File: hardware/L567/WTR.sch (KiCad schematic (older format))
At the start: 14 parts, among them Q4 2N3014

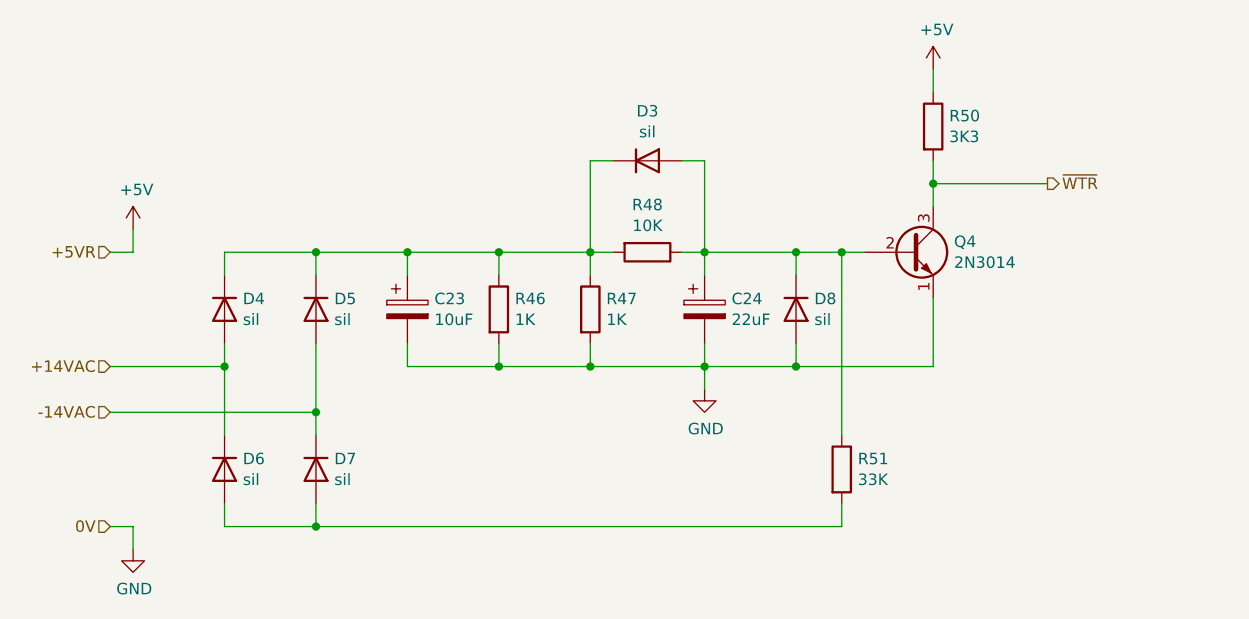
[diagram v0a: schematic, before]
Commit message: some power supply updates
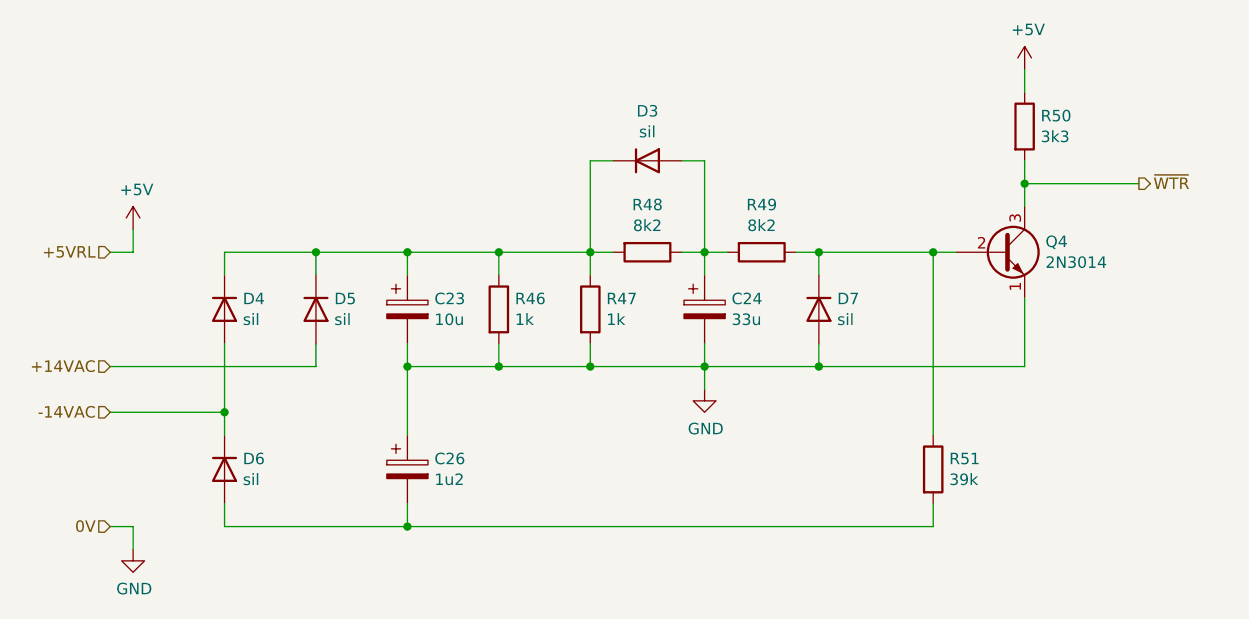
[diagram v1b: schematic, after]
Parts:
- removed D7: sil, symbol Device:D
- added C26: 1u2, symbol Device:CP
- added R49: 8k2, symbol Device:R
- C23: value 10uF -> 10u
- C24: value 22uF -> 33u; Partnumber 330-4015 -> 330-4019
- R46, R47: value 1K -> 1k
- R48: value 10K -> 8k2; Partnumber 330-4010 -> (none); Tolerance (none) -> 5%
- R50: value 3K3 -> 3k3
- R51: value 33K -> 39k; Tolerance (none) -> 5%
- renumbered D8 to D7
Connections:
- net +14VAC: now also D5.2 (A); no longer D4.2 (A), D6.1 (K)
- net -14VAC: now also D4.2 (A), D6.1 (K); no longer D5.2 (A)
- net GND: now also C26.1
- net at D6.2 (A), R51.2: now also C26.2
- net at C24.1, D3.2 (A), R48.1: now also R49.2; no longer D7.1 (K), Q4.2 (B), R51.1
- new net: D7.1 (K), Q4.2 (B), R49.1, R51.1
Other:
- moved on the sheet: D7, Q4, R50, R51
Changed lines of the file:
@@
 $Descr A4 11693 8268
 encoding utf-8
-Sheet 2 2
+Sheet 2 4
 Title ""
 Date ""
@@
 	6000 2600 6100 2600
 Wire Wire Line
-	6100 3000 6500 3000
+	6500 3000 6600 3000
 Connection ~ 6100 3000
 Wire Wire Line
 	6100 3000 6100 3100
 Wire Wire Line
-	6500 3000 6700 3000
-Connection ~ 6500 3000
-Wire Wire Line
-	6500 3000 6500 3100
+	6600 3000 7100 3000
+Connection ~ 6600 3000
+Wire Wire Line
+	6600 3000 6600 3100
 Wire Wire Line
 	6000 3000 6100 3000
@@
 Wire Wire Line
 	5700 3000 5600 3000
-Connection ~ 6500 3500
-Wire Wire Line
-	7100 3500 7100 3200
-Wire Wire Line
-	6500 3500 7100 3500
+Connection ~ 6600 3500
+Wire Wire Line
+	7500 3500 7500 3200
+Wire Wire Line
+	6600 3500 7500 3500
 Connection ~ 6100 3500
 Wire Wire Line
-	6500 3500 6500 3400
-Wire Wire Line
-	6100 3500 6500 3500
+	6600 3500 6600 3400
+Wire Wire Line
+	6100 3500 6600 3500
 Connection ~ 5600 3500
 Wire Wire Line
@@
 	4800 3000 4800 3100
 Text HLabel 3500 3000 0    50   Input ~ 0
-+5VR
++5VRL
 Text HLabel 3500 4200 0    50   Input ~ 0
 0V
-Text HLabel 7600 2700 2    50   Output ~ 0
+Text HLabel 8000 2700 2    50   Output ~ 0
 ~WTR
 $Comp
 L Device:R R50
 U 1 1 6056D046
-P 7100 2450
-F 0 "R50" H 7170 2496 50  0000 L CNN
-F 1 "3K3" H 7170 2405 50  0000 L CNN
-F 2 "" V 7030 2450 50  0001 C CNN
-F 3 "~" H 7100 2450 50  0001 C CNN
-F 4 "330-3033" H 7100 2450 50  0001 C CNN "Partnumber"
-F 5 "1/4W" H 7100 2450 50  0001 C CNN "Power"
-	1    7100 2450
+P 7500 2450
+F 0 "R50" H 7570 2496 50  0000 L CNN
+F 1 "3k3" H 7570 2405 50  0000 L CNN
+F 2 "" V 7430 2450 50  0001 C CNN
+F 3 "~" H 7500 2450 50  0001 C CNN
+F 4 "330-3033" H 7500 2450 50  0001 C CNN "Partnumber"
+F 5 "1/4W" H 7500 2450 50  0001 C CNN "Power"
+	1    7500 2450
 	1    0    0    -1
 $EndComp
@@
 L Device:Q_NPN_EBC Q4
 U 1 1 6056C773
-P 7000 3000
-F 0 "Q4" H 7191 3046 50  0000 L CNN
-F 1 "2N3014" H 7191 2955 50  0000 L CNN
-F 2 "" H 7200 3100 50  0001 C CNN
-F 3 "~" H 7000 3000 50  0001 C CNN
-F 4 "375-0017" H 7000 3000 50  0001 C CNN "Partnumber"
-	1    7000 3000
+P 7400 3000
+F 0 "Q4" H 7591 3046 50  0000 L CNN
+F 1 "2N3014" H 7591 2955 50  0000 L CNN
+F 2 "" H 7600 3100 50  0001 C CNN
+F 3 "~" H 7400 3000 50  0001 C CNN
+F 4 "375-0017" H 7400 3000 50  0001 C CNN "Partnumber"
+	1    7400 3000
 	1    0    0    -1
 $EndComp
@@
 L Device:R R51
 U 1 1 6056AAF1
-P 6700 3950
-F 0 "R51" H 6770 3996 50  0000 L CNN
-F 1 "33K" H 6770 3905 50  0000 L CNN
-F 2 "" V 6630 3950 50  0001 C CNN
-F 3 "~" H 6700 3950 50  0001 C CNN
-F 4 "330-4033" H 6700 3950 50  0001 C CNN "Partnumber"
-F 5 "1/4W" H 6700 3950 50  0001 C CNN "Power"
-	1    6700 3950
+P 7100 3950
+F 0 "R51" H 7170 3996 50  0000 L CNN
+F 1 "39k" H 7170 3905 50  0000 L CNN
+F 2 "" V 7030 3950 50  0001 C CNN
+F 3 "~" H 7100 3950 50  0001 C CNN
+F 4 "330-4033" H 7100 3950 50  0001 C CNN "Partnumber"
+F 5 "1/4W" H 7100 3950 50  0001 C CNN "Power"
+F 6 "5%" H 7100 3950 50  0001 C CNN "Tolerance"
+	1    7100 3950
 	1    0    0    -1
 $EndComp
@@
 P 4800 3250
 F 0 "C23" H 4918 3296 50  0000 L CNN
-F 1 "10uF" H 4918 3205 50  0000 L CNN
+F 1 "10u" H 4918 3205 50  0000 L CNN
 F 2 "" H 4838 3100 50  0001 C CNN
 F 3 "~" H 4800 3250 50  0001 C CNN
@@
 $EndComp
 $Comp
-L Device:D D8
+L Device:D D7
 U 1 1 6056397D
-P 6500 3250
-F 0 "D8" V 6454 3330 50  0000 L CNN
-F 1 "sil" V 6545 3330 50  0000 L CNN
-F 2 "" H 6500 3250 50  0001 C CNN
-F 3 "~" H 6500 3250 50  0001 C CNN
-F 4 "380-1001" H 6500 3250 50  0001 C CNN "Partnumber"
-F 5 "Silicium" H 6500 3250 50  0001 C CNN "Technology"
-	1    6500 3250
+P 6600 3250
+F 0 "D7" V 6554 3330 50  0000 L CNN
+F 1 "sil" V 6645 3330 50  0000 L CNN
+F 2 "" H 6600 3250 50  0001 C CNN
+F 3 "~" H 6600 3250 50  0001 C CNN
+F 4 "380-1001" H 6600 3250 50  0001 C CNN "Partnumber"
+F 5 "Silicium" H 6600 3250 50  0001 C CNN "Technology"
+	1    6600 3250
 	0    1    1    0
 $EndComp
@@
 P 5850 3000
 F 0 "R48" V 5643 3000 50  0000 C CNN
-F 1 "10K" V 5734 3000 50  0000 C CNN
+F 1 "8k2" V 5734 3000 50  0000 C CNN
 F 2 "" V 5780 3000 50  0001 C CNN
 F 3 "~" H 5850 3000 50  0001 C CNN
-F 4 "330-4010" H 5850 3000 50  0001 C CNN "Partnumber"
+F 4 "" H 5850 3000 50  0001 C CNN "Partnumber"
 F 5 "1/4W" H 5850 3000 50  0001 C CNN "Power"
+F 6 "5%" H 5850 3000 50  0001 C CNN "Tolerance"
 	1    5850 3000
 	0    1    1    0
@@
 P 5600 3250
 F 0 "R47" H 5670 3296 50  0000 L CNN
-F 1 "1K" H 5670 3205 50  0000 L CNN
+F 1 "1k" H 5670 3205 50  0000 L CNN
 F 2 "" V 5530 3250 50  0001 C CNN
 F 3 "~" H 5600 3250 50  0001 C CNN
@@
 P 5200 3250
 F 0 "R46" H 5270 3296 50  0000 L CNN
-F 1 "1K" H 5270 3205 50  0000 L CNN
+F 1 "1k" H 5270 3205 50  0000 L CNN
 F 2 "" V 5130 3250 50  0001 C CNN
 F 3 "~" H 5200 3250 50  0001 C CNN
@@
 P 6100 3250
 F 0 "C24" H 6218 3296 50  0000 L CNN
-F 1 "22uF" H 6218 3205 50  0000 L CNN
+F 1 "33u" H 6218 3205 50  0000 L CNN
 F 2 "" H 6138 3100 50  0001 C CNN
 F 3 "~" H 6100 3250 50  0001 C CNN
-F 4 "330-4015" H 6100 3250 50  0001 C CNN "Partnumber"
+F 4 "330-4019" H 6100 3250 50  0001 C CNN "Partnumber"
 F 5 "Tantalum" H 6100 3250 50  0001 C CNN "Technology"
 F 6 "15V" H 6100 3250 50  0001 C CNN "Voltage"
@@
 $EndComp
 Wire Wire Line
-	4400 3700 4400 3800
-Connection ~ 4400 3700
-Wire Wire Line
-	3500 3700 4400 3700
-Wire Wire Line
-	4000 3500 4000 3800
-Connection ~ 4000 3500
-Wire Wire Line
-	3500 3500 4000 3500
-Wire Wire Line
-	4400 3400 4400 3700
-Wire Wire Line
-	4400 4200 4400 4100
-Wire Wire Line
-	4000 4200 4400 4200
+	3500 3500 4400 3500
+Wire Wire Line
+	4000 3700 4000 3800
+Connection ~ 4000 3700
+Wire Wire Line
+	3500 3700 4000 3700
+Wire Wire Line
+	4400 3400 4400 3500
 Wire Wire Line
 	4000 4100 4000 4200
 Wire Wire Line
-	4000 3400 4000 3500
+	4000 3400 4000 3700
 Wire Wire Line
 	4400 3000 4400 3100
@@
 Wire Wire Line
 	4000 3100 4000 3000
-$Comp
-L Device:D D7
-U 1 1 6055D71C
-P 4400 3950
-F 0 "D7" V 4354 4030 50  0000 L CNN
-F 1 "sil" V 4445 4030 50  0000 L CNN
-F 2 "" H 4400 3950 50  0001 C CNN
-F 3 "~" H 4400 3950 50  0001 C CNN
-F 4 "380-1004" H 4400 3950 50  0001 C CNN "Partnumber"
-F 5 "Silicium" H 4400 3950 50  0001 C CNN "Technology"
-	1    4400 3950
-	0    1    1    0
-$EndComp
 $Comp
 L Device:D D6
@@
 +14VAC
 Wire Wire Line
-	6700 3000 6700 3800
-Connection ~ 6700 3000
-Wire Wire Line
-	6700 3000 6800 3000
+	7100 3000 7100 3800
+Connection ~ 7100 3000
+Wire Wire Line
+	7100 3000 7200 3000
 Wire Wire Line
 	6100 3500 6100 3600
 Wire Wire Line
-	6700 4100 6700 4200
-Wire Wire Line
-	6700 4200 4400 4200
-Connection ~ 4400 4200
+	7100 4100 7100 4200
 $Comp
 L power:+5V #PWR0102
@@
 L power:+5V #PWR0104
 U 1 1 605DC71E
-P 7100 2200
-F 0 "#PWR0104" H 7100 2050 50  0001 C CNN
-F 1 "+5V" H 7115 2373 50  0000 C CNN
-F 2 "" H 7100 2200 50  0001 C CNN
-F 3 "" H 7100 2200 50  0001 C CNN
-	1    7100 2200
-	1    0    0    -1
-$EndComp
-Wire Wire Line
-	7100 2200 7100 2300
-Wire Wire Line
-	7100 2600 7100 2700
-Wire Wire Line
-	7100 2700 7600 2700
-Connection ~ 7100 2700
-Wire Wire Line
-	7100 2700 7100 2800
+P 7500 2200
+F 0 "#PWR0104" H 7500 2050 50  0001 C CNN
+F 1 "+5V" H 7515 2373 50  0000 C CNN
+F 2 "" H 7500 2200 50  0001 C CNN
+F 3 "" H 7500 2200 50  0001 C CNN
+	1    7500 2200
+	1    0    0    -1
+$EndComp
+Wire Wire Line
+	7500 2200 7500 2300
+Wire Wire Line
+	7500 2600 7500 2700
+Wire Wire Line
+	7500 2700 8000 2700
+Connection ~ 7500 2700
+Wire Wire Line
+	7500 2700 7500 2800
+Wire Wire Line
+	7100 4200 4800 4200
+$Comp
+L Device:CP C26
+U 1 1 607B5AED
+P 4800 3950
+F 0 "C26" H 4918 3996 50  0000 L CNN
+F 1 "1u2" H 4918 3905 50  0000 L CNN
+F 2 "" H 4838 3800 50  0001 C CNN
+F 3 "~" H 4800 3950 50  0001 C CNN
+F 4 "" H 4800 3950 50  0001 C CNN "Partnumber"
+F 5 "Tantalum" H 4800 3950 50  0001 C CNN "Technology"
+F 6 "35V" H 4800 3950 50  0001 C CNN "Voltage"
+	1    4800 3950
+	1    0    0    -1
+$EndComp
+Wire Wire Line
+	4800 3500 4800 3800
+Connection ~ 4800 3500
+Wire Wire Line
+	4800 4100 4800 4200
+Wire Wire Line
+	4000 4200 4800 4200
+$Comp
+L Device:R R49
+U 1 1 607C003B
+P 6350 3000
+F 0 "R49" V 6143 3000 50  0000 C CNN
+F 1 "8k2" V 6234 3000 50  0000 C CNN
+F 2 "" V 6280 3000 50  0001 C CNN
+F 3 "~" H 6350 3000 50  0001 C CNN
+F 4 "" H 6350 3000 50  0001 C CNN "Partnumber"
+F 5 "1/4W" H 6350 3000 50  0001 C CNN "Power"
+F 6 "5%" H 6350 3000 50  0001 C CNN "Tolerance"
+	1    6350 3000
+	0    1    1    0
+$EndComp
+Connection ~ 4800 4200
+Wire Wire Line
+	6100 3000 6200 3000
 $EndSCHEMATC
